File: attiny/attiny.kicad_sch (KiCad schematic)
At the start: 11 parts, among them J1 arduino, J2 esp32, J3 cavalier, J4 Conn_01x01, U1 ATtiny85V-10S

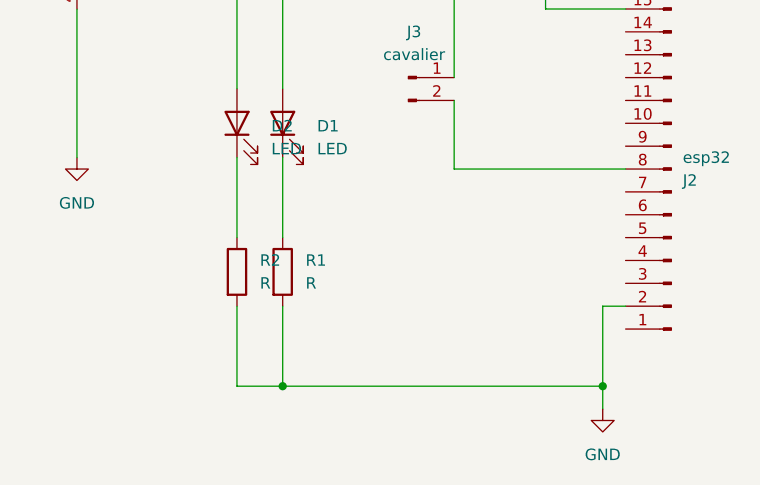
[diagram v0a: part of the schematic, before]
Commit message: mise a jour reference resistance avec ref jlcsc
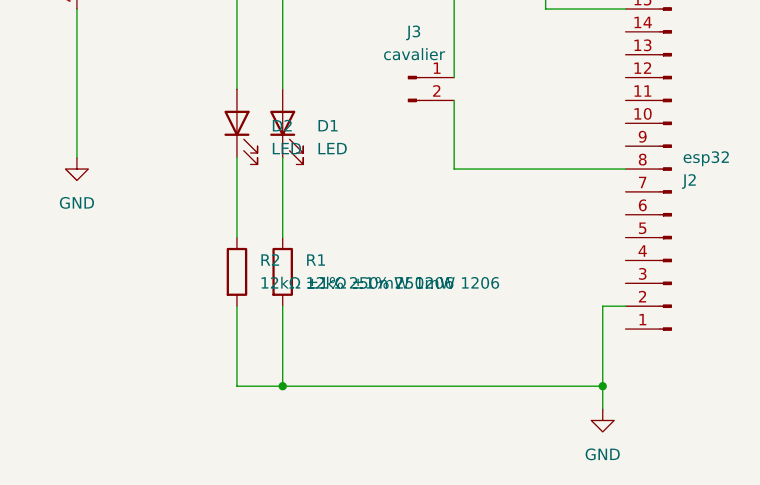
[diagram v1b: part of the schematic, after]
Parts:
- R1, R2: value R -> 12kΩ ±1% 250mW 1206
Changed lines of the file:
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@@
 			)
 		)
-		(property "Value" "R"
+		(property "Value" "12kΩ ±1% 250mW 1206"
 			(at 156.21 139.6999 0)
 			(effects
@@
 			)
 		)
-		(property "Value" "R"
+		(property "Value" "12kΩ ±1% 250mW 1206"
 			(at 151.13 139.6999 0)
 			(effects
